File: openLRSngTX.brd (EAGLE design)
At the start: 50 x 40 mm, 29 parts, among them IC1 RFM23BPSMD, J1 AVR_SPI_PRG_6PTH, Q1 MMBT2222, U1 ATMEGA328P, X1 BU-SMA-V, Y1 16MHz

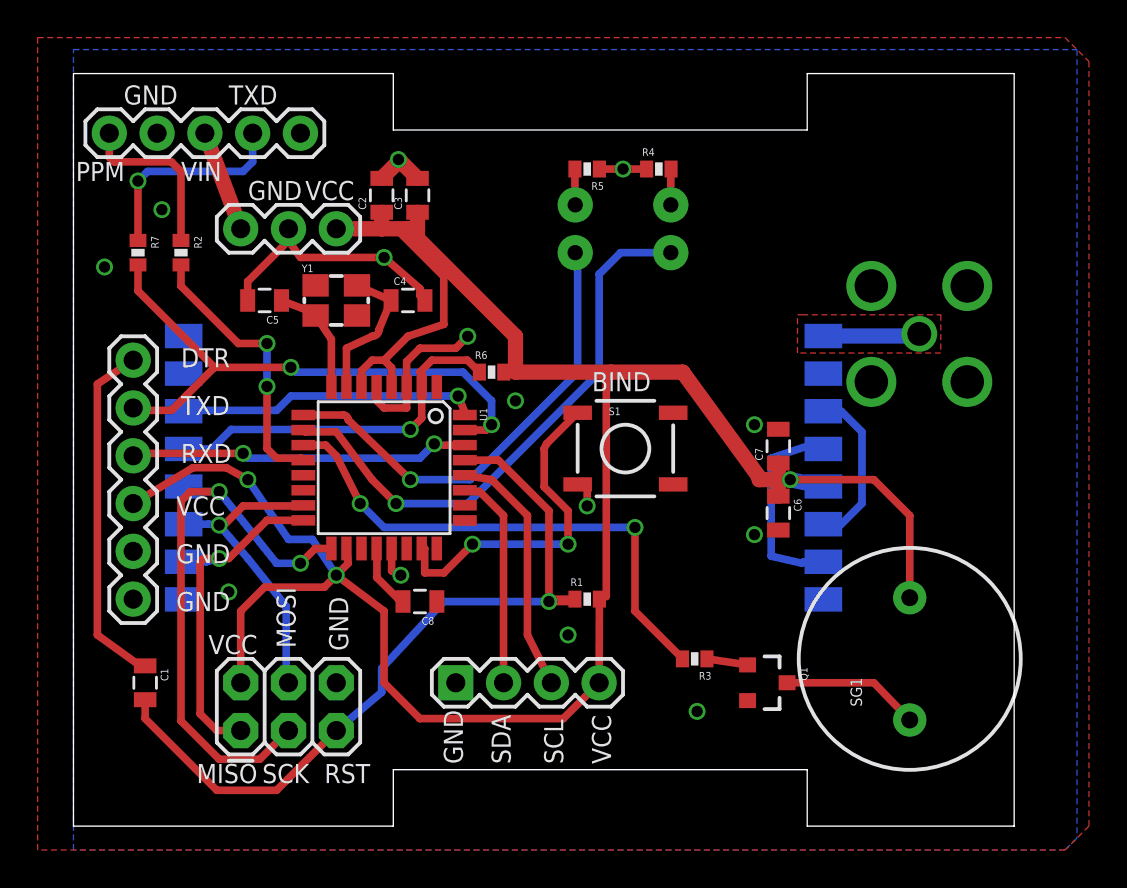
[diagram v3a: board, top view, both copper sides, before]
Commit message: Correct button placement, thanks remspoor =)
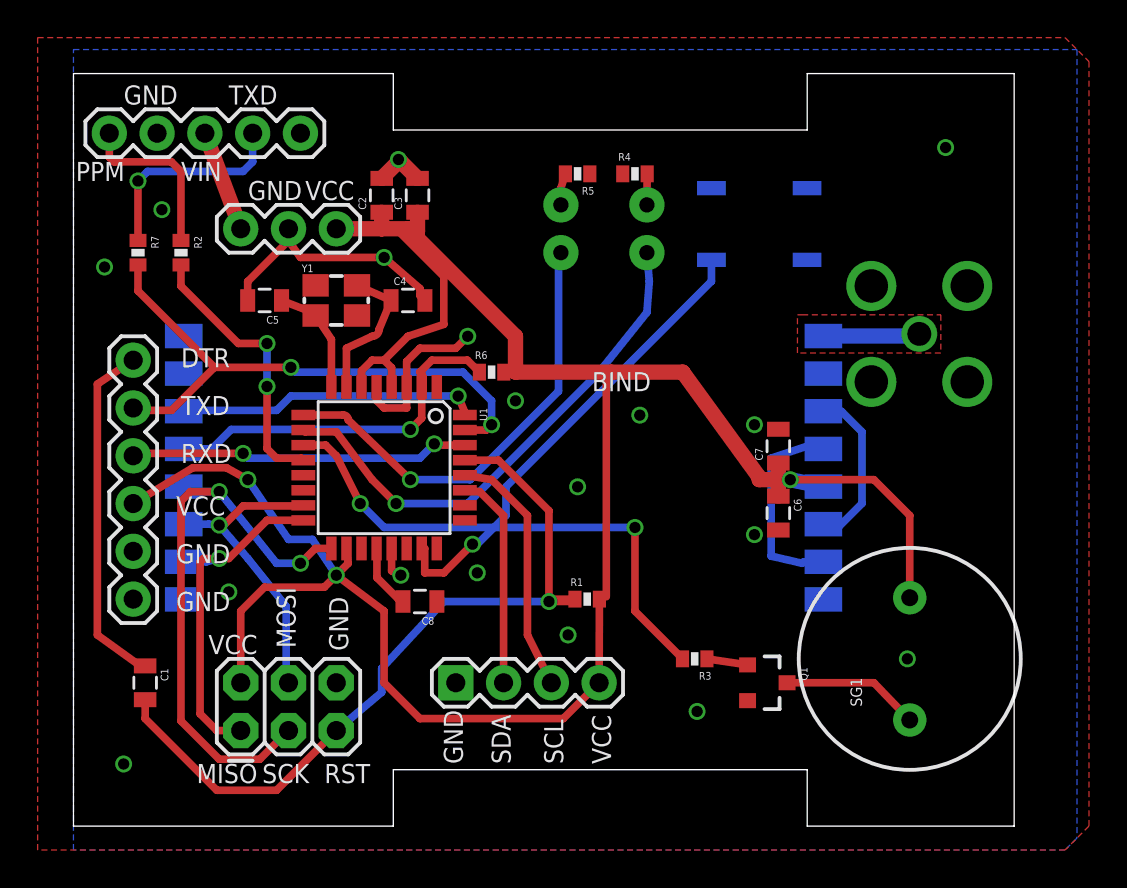
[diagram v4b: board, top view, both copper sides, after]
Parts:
- moved S1 13.9 mm to (35.8, 32.0), flipped to the bottom, turned to 180 degrees
- moved R4 1.30 mm to (29.2, 34.7)
- moved LED1 1.27 mm to (29.8, 31.8)
- moved LED2 0.76 mm to (25.3, 31.8)
- moved R5 0.57 mm to (26.2, 34.7)
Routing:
- net N$15: track 17.9 -> 25.1 mm, vias 2 -> 1
- net GND: track 31.0 -> 26.8 mm, vias 14 -> 18
- net N$7: track 29.9 -> 27.7 mm
- net N$10: track 1.91 -> 1.69 mm, vias 1 -> 0
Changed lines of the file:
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@@
 <element name="R2" library="SparkFun-Resistors" package="0402-RES" value="1k" x="5.08" y="30.48" rot="R270"/>
 <element name="R3" library="SparkFun-Resistors" package="0402-RES" value="1k" x="32.385" y="8.89" rot="R180"/>
-<element name="R4" library="SparkFun-Resistors" package="0402-RES" value="220R" x="30.48" y="34.925"/>
-<element name="R5" library="SparkFun-Resistors" package="0402-RES" value="220R" x="26.67" y="34.925" rot="R180"/>
-<element name="LED1" library="SparkFun-LED" package="LED3MM" value="RED" x="31.115" y="31.75" smashed="yes" rot="MR90"/>
-<element name="LED2" library="SparkFun-LED" package="LED3MM" value="GRN" x="26.035" y="31.75" smashed="yes" rot="MR90"/>
+<element name="R4" library="SparkFun-Resistors" package="0402-RES" value="220R" x="29.21" y="34.671"/>
+<element name="R5" library="SparkFun-Resistors" package="0402-RES" value="220R" x="26.162" y="34.671" rot="R180"/>
+<element name="LED1" library="SparkFun-LED" package="LED3MM" value="RED" x="29.845" y="31.75" smashed="yes" rot="MR90"/>
+<element name="LED2" library="SparkFun-LED" package="LED3MM" value="GRN" x="25.273" y="31.75" smashed="yes" rot="MR90"/>
 <element name="SG1" library="SparkFun-Electromechanical" package="BUZZER-12MM" value="BUZZERPTH" x="43.815" y="8.89" smashed="yes" rot="R90">
 <attribute name="NAME" x="41.275" y="6.35" size="0.6096" layer="25" ratio="10" rot="R90"/>
@@
 <element name="R6" library="SparkFun-Resistors" package="0402-RES" value="1k" x="21.59" y="24.13"/>
 <element name="C8" library="SparkFun-Capacitors" package="0805" value="100n" x="17.78" y="11.938" rot="R180"/>
-<element name="S1" library="SparkFun-Electromechanical" package="TACTILE_SWITCH_SMD" value="SWITCH-MOMENTARY-2SMD" x="28.702" y="20.066"/>
+<element name="S1" library="SparkFun-Electromechanical" package="TACTILE_SWITCH_SMD" value="SWITCH-MOMENTARY-2SMD" x="35.814" y="32.004" rot="MR180"/>
 <element name="R7" library="SparkFun-Resistors" package="0402-RES" value="1k" x="2.794" y="30.48" rot="R270"/>
 </elements>
@@
 <wire x1="16.275" y1="14.7574" x2="16.275" y2="13.57" width="0.4064" layer="1"/>
 <wire x1="16.275" y1="13.57" x2="16.764" y2="13.335" width="0.4064" layer="1"/>
-<via x="28.575" y="34.925" extent="1-16" drill="0.6"/>
-<wire x1="27.32" y1="34.925" x2="28.575" y2="34.925" width="0.4064" layer="1"/>
-<wire x1="29.83" y1="34.925" x2="28.575" y2="34.925" width="0.4064" layer="1"/>
 <contactref element="C6" pad="2"/>
 <contactref element="C7" pad="2"/>
@@
 <via x="4.064" y="32.766" extent="1-16" drill="0.6"/>
 <via x="25.654" y="10.16" extent="1-16" drill="0.6"/>
-<via x="26.67" y="17.018" extent="1-16" drill="0.6"/>
-<wire x1="26.162" y1="18.161" x2="26.67" y2="18.161" width="0.4064" layer="1"/>
-<wire x1="26.67" y1="18.161" x2="26.67" y2="17.018" width="0.4064" layer="1"/>
+<via x="26.162" y="18.034" extent="1-16" drill="0.6"/>
 <via x="1.016" y="29.718" extent="1-16" drill="0.6"/>
 <via x="22.86" y="22.606" extent="1-16" drill="0.6"/>
+<via x="29.464" y="21.844" extent="1-16" drill="0.6"/>
+<via x="43.688" y="8.89" extent="1-16" drill="0.6"/>
+<via x="20.828" y="13.462" extent="1-16" drill="0.6"/>
+<via x="2.032" y="3.302" extent="1-16" drill="0.6"/>
+<via x="45.72" y="36.068" extent="1-16" drill="0.6"/>
 </signal>
 <signal name="VCC">
@@
 <contactref element="LED1" pad="A"/>
 <contactref element="U1" pad="10"/>
-<wire x1="27.305" y1="29.337" x2="27.305" y2="24.13" width="0.4064" layer="16"/>
+<wire x1="29.845" y1="27.305" x2="27.305" y2="24.13" width="0.4064" layer="16"/>
 <wire x1="27.305" y1="24.13" x2="20.32" y2="17.145" width="0.4064" layer="16"/>
 <wire x1="20.32" y1="17.145" x2="16.51" y2="17.145" width="0.4064" layer="16"/>
@@
 <wire x1="13.335" y1="20.955" x2="11.6774" y2="20.955" width="0.4064" layer="1"/>
 <wire x1="11.6774" y1="20.955" x2="11.5824" y2="21.05" width="0.4064" layer="1"/>
-<wire x1="27.305" y1="29.337" x2="28.448" y2="30.48" width="0.4064" layer="16"/>
-<wire x1="28.448" y1="30.48" x2="31.115" y2="30.48" width="0.4064" layer="16"/>
+<wire x1="29.845" y1="27.305" x2="29.972" y2="28.956" width="0.4064" layer="16"/>
+<wire x1="29.972" y1="28.956" x2="29.845" y2="30.48" width="0.4064" layer="16"/>
 </signal>
 <signal name="N$8">
@@
 <via x="17.272" y="18.415" extent="1-16" drill="0.6"/>
 <wire x1="17.272" y1="18.415" x2="20.447" y2="18.415" width="0.4064" layer="16"/>
-<wire x1="20.447" y1="18.415" x2="26.162" y2="24.13" width="0.4064" layer="16"/>
-<wire x1="26.162" y1="24.13" x2="26.162" y2="30.353" width="0.4064" layer="16"/>
-<wire x1="26.162" y1="30.353" x2="26.035" y2="30.48" width="0.4064" layer="16"/>
+<wire x1="20.447" y1="18.415" x2="25.146" y2="23.114" width="0.4064" layer="16"/>
+<wire x1="25.146" y1="23.114" x2="25.146" y2="30.353" width="0.4064" layer="16"/>
+<wire x1="25.146" y1="30.353" x2="25.273" y2="30.48" width="0.4064" layer="16"/>
 </signal>
 <signal name="N$9">
 <contactref element="LED1" pad="K"/>
 <contactref element="R4" pad="2"/>
-<wire x1="31.115" y1="33.02" x2="31.115" y2="34.91" width="0.4064" layer="1"/>
-<wire x1="31.115" y1="34.91" x2="31.13" y2="34.925" width="0.4064" layer="1"/>
+<wire x1="29.845" y1="33.02" x2="29.845" y2="33.132" width="0.4064" layer="1"/>
+<wire x1="29.845" y1="33.132" x2="29.86" y2="34.671" width="0.4064" layer="1"/>
 </signal>
 <signal name="N$10">
 <contactref element="LED2" pad="K"/>
 <contactref element="R5" pad="2"/>
-<wire x1="26.02" y1="34.925" x2="26.02" y2="33.035" width="0.4064" layer="1"/>
-<wire x1="26.02" y1="33.035" x2="26.035" y2="33.02" width="0.4064" layer="16"/>
-<via x="26.02" y="33.035" extent="1-16" drill="0.6"/>
+<wire x1="25.512" y1="34.671" x2="25.273" y2="33.909" width="0.4064" layer="1"/>
+<wire x1="25.273" y1="33.909" x2="25.273" y2="33.02" width="0.4064" layer="1"/>
 </signal>
 <signal name="N$11">
@@
 <wire x1="19.05" y1="13.462" x2="20.574" y2="14.986" width="0.4064" layer="1"/>
 <via x="20.574" y="14.986" extent="1-16" drill="0.6"/>
-<wire x1="20.574" y1="14.986" x2="25.654" y2="14.986" width="0.4064" layer="16"/>
-<via x="25.654" y="14.986" extent="1-16" drill="0.6"/>
-<wire x1="25.654" y1="14.986" x2="25.654" y2="16.764" width="0.4064" layer="1"/>
-<wire x1="25.654" y1="16.764" x2="24.384" y2="18.034" width="0.4064" layer="1"/>
-<wire x1="24.384" y1="18.034" x2="24.384" y2="20.066" width="0.4064" layer="1"/>
-<wire x1="24.384" y1="20.066" x2="24.511" y2="20.32" width="0.4064" layer="1"/>
-<wire x1="24.511" y1="20.32" x2="26.162" y2="21.971" width="0.4064" layer="1"/>
+<wire x1="20.574" y1="14.986" x2="20.828" y2="14.986" width="0.4064" layer="16"/>
+<wire x1="20.828" y1="14.986" x2="22.352" y2="16.51" width="0.4064" layer="16"/>
+<wire x1="22.352" y1="16.51" x2="22.352" y2="18.034" width="0.4064" layer="16"/>
+<wire x1="22.352" y1="18.034" x2="33.274" y2="28.956" width="0.4064" layer="16"/>
+<wire x1="33.274" y1="28.956" x2="33.274" y2="30.099" width="0.4064" layer="16"/>
 </signal>
 <signal name="N$16">
